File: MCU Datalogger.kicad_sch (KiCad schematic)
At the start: 25 parts, among them U1 24LC1025, U2 DS1337S+, U3 24LC1025, U4 ATMEGA328P-AU, Y1 32.768 KHz, Y2 16MHz

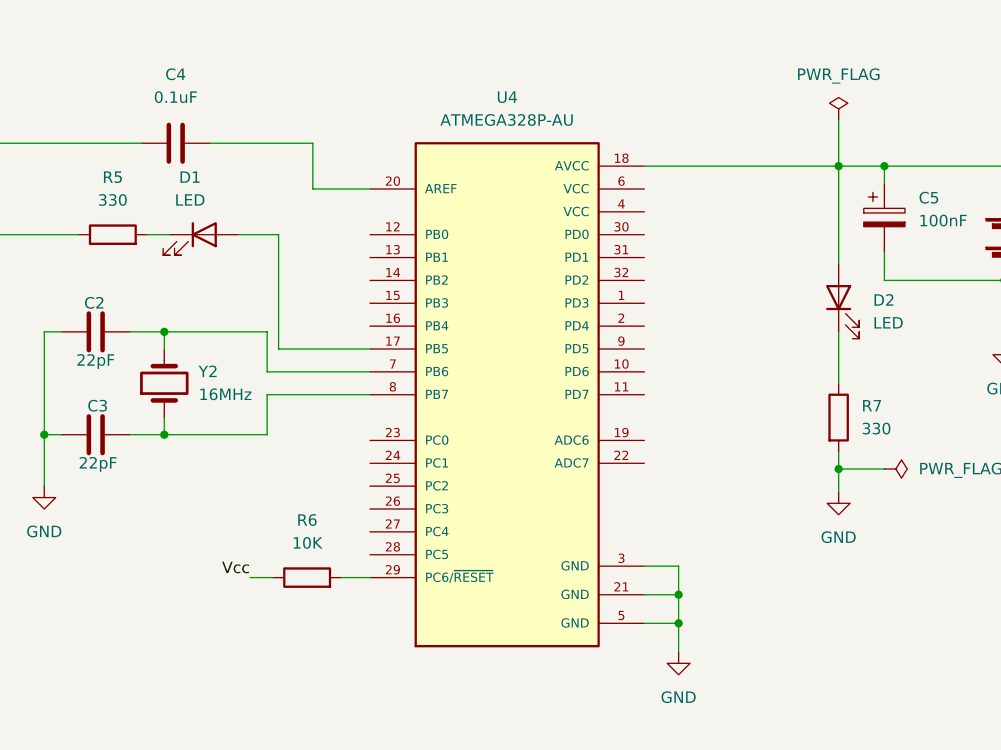
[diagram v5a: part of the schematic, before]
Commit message: finished wiring of main sheet
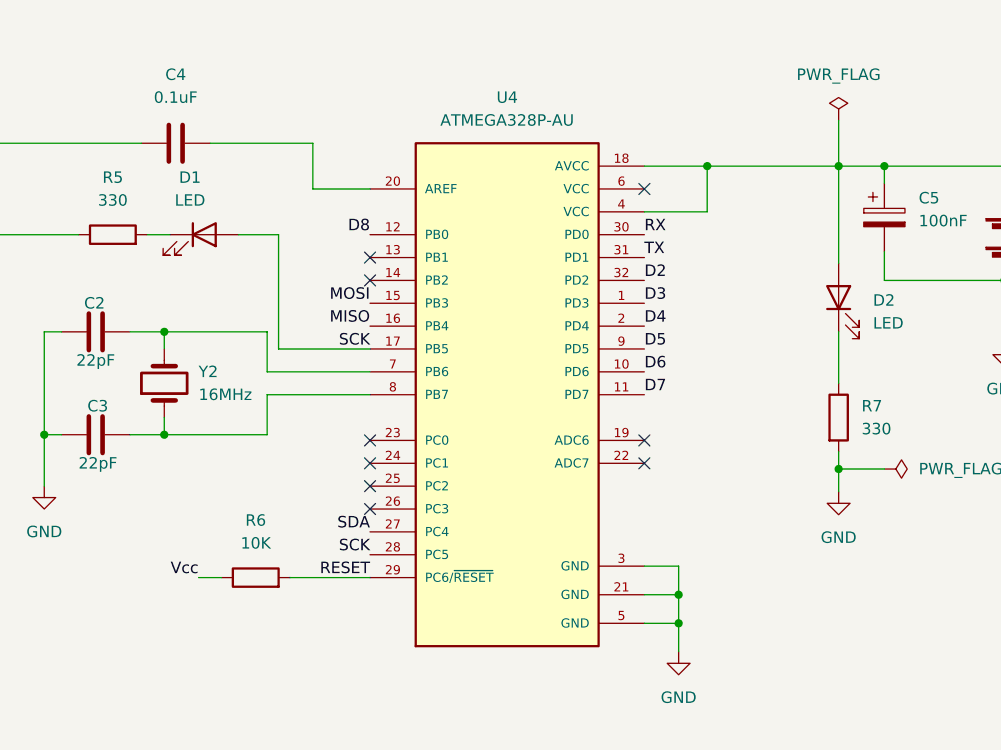
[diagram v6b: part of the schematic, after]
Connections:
- net SCK: now also D1.2 (A), U4.17 (PB5), U4.28 (PC5)
- net SDA: now also U4.27 (PC4)
- net at BT1.1 (+), C5.1, D2.2 (A)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: now also U4.4 (VCC)
- net D3: now reaches U4.1 (PD3)
- net D6: now reaches U4.10 (PD6)
- net D7: now reaches U4.11 (PD7)
- net D8: now reaches U4.12 (PB0)
- net MOSI: now reaches U4.15 (PB3)
- net MISO: now reaches U4.16 (PB4)
- net D4: now reaches U4.2 (PD4)
- net RESET: now reaches R6.2, U4.29 (PC6/~{RESET})
- net RX: now reaches U4.30 (PD0)
- net TX: now reaches U4.31 (PD1)
- net D2: now reaches U4.32 (PD2)
- net D5: now reaches U4.9 (PD5)
- no-connect marks 0 -> 9
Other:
- moved on the sheet: R6
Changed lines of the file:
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@@
   (junction (at 155.575 49.53) (diameter 0) (color 0 0 0 0)
   )
+  (junction (at 238.125 41.91) (diameter 0) (color 0 0 0 0)
+  )
   (junction (at 271.145 54.61) (diameter 0) (color 0 0 0 0)
   )
   (junction (at 88.9 26.67) (diameter 0) (color 0 0 0 0)
   )
+  (no_connect (at 200.66 52.07))
+  (no_connect (at 200.66 54.61))
+  (no_connect (at 200.66 72.39))
+  (no_connect (at 200.66 74.93))
+  (no_connect (at 200.66 77.47))
+  (no_connect (at 200.66 80.01))
+  (no_connect (at 231.14 44.45))
+  (no_connect (at 231.14 72.39))
+  (no_connect (at 231.14 74.93))
   (wire (pts (xy 234.95 92.71) (xy 234.95 95.885))
     (stroke (width 0) (type default) (color 0 0 0 0))
@@
     (stroke (width 0) (type default) (color 0 0 0 0))
   )
-  (wire (pts (xy 187.325 87.63) (xy 189.865 87.63))
+  (wire (pts (xy 181.61 87.63) (xy 184.15 87.63))
     (stroke (width 0) (type default) (color 0 0 0 0))
   )
@@
     (stroke (width 0) (type default) (color 0 0 0 0))
   )
+  (wire (pts (xy 231.14 46.99) (xy 238.125 46.99))
+    (stroke (width 0) (type default) (color 0 0 0 0))
+  )
   (wire (pts (xy 99.06 34.29) (xy 99.06 45.72))
     (stroke (width 0) (type default) (color 0 0 0 0))
@@
     (stroke (width 0) (type default) (color 0 0 0 0))
   )
+  (wire (pts (xy 238.125 41.91) (xy 252.73 41.91))
+    (stroke (width 0) (type default) (color 0 0 0 0))
+  )
   (wire (pts (xy 74.93 35.56) (xy 88.9 35.56))
     (stroke (width 0) (type default) (color 0 0 0 0))
@@
     (stroke (width 0) (type default) (color 0 0 0 0))
   )
-  (wire (pts (xy 197.485 87.63) (xy 200.66 87.63))
+  (wire (pts (xy 191.77 87.63) (xy 200.66 87.63))
     (stroke (width 0) (type default) (color 0 0 0 0))
   )
@@
     (stroke (width 0) (type default) (color 0 0 0 0))
   )
-  (wire (pts (xy 231.14 41.91) (xy 252.73 41.91))
+  (wire (pts (xy 231.14 41.91) (xy 238.125 41.91))
     (stroke (width 0) (type default) (color 0 0 0 0))
   )
@@
     (stroke (width 0) (type default) (color 0 0 0 0))
   )
+  (wire (pts (xy 238.125 46.99) (xy 238.125 41.91))
+    (stroke (width 0) (type default) (color 0 0 0 0))
+  )
   (wire (pts (xy 164.465 71.755) (xy 164.465 77.47))
     (stroke (width 0) (type default) (color 0 0 0 0))
@@
     (effects (font (size 1.27 1.27)) (justify right bottom))
   )
+  (label "D5" (at 231.14 62.23 0)
+    (effects (font (size 1.27 1.27)) (justify left bottom))
+  )
+  (label "D6" (at 231.14 64.77 0)
+    (effects (font (size 1.27 1.27)) (justify left bottom))
+  )
   (label "SCK" (at 86.36 177.8 180)
     (effects (font (size 1.27 1.27)) (justify right bottom))
   )
+  (label "TX" (at 231.14 52.07 0)
+    (effects (font (size 1.27 1.27)) (justify left bottom))
+  )
+  (label "SDA" (at 200.66 82.55 180)
+    (effects (font (size 1.27 1.27)) (justify right bottom))
+  )
   (label "Vcc" (at 52.07 172.72 180)
     (effects (font (size 1.27 1.27)) (justify right bottom))
   )
+  (label "SCK" (at 200.66 85.09 180)
+    (effects (font (size 1.27 1.27)) (justify right bottom))
+  )
+  (label "MISO" (at 200.66 59.69 180)
+    (effects (font (size 1.27 1.27)) (justify right bottom))
+  )
   (label "Vcc" (at 22.86 167.64 180)
     (effects (font (size 1.27 1.27)) (justify right bottom))
   )
+  (label "D4" (at 231.14 59.69 0)
+    (effects (font (size 1.27 1.27)) (justify left bottom))
+  )
+  (label "RESET" (at 200.66 87.63 180)
+    (effects (font (size 1.27 1.27)) (justify right bottom))
+  )
   (label "Vcc" (at 33.02 162.56 0)
     (effects (font (size 1.27 1.27)) (justify left bottom))
   )
+  (label "RX" (at 231.14 49.53 0)
+    (effects (font (size 1.27 1.27)) (justify left bottom))
+  )
+  (label "MOSI" (at 200.66 57.15 180)
+    (effects (font (size 1.27 1.27)) (justify right bottom))
+  )
   (label "Vcc" (at 22.86 172.72 180)
     (effects (font (size 1.27 1.27)) (justify right bottom))
@@
     (effects (font (size 1.27 1.27)) (justify right bottom))
   )
+  (label "D7" (at 231.14 67.31 0)
+    (effects (font (size 1.27 1.27)) (justify left bottom))
+  )
   (label "SDA" (at 36.83 39.37 180)
     (effects (font (size 1.27 1.27)) (justify right bottom))
@@
     (effects (font (size 1.27 1.27)) (justify right bottom))
   )
+  (label "D3" (at 231.14 57.15 0)
+    (effects (font (size 1.27 1.27)) (justify left bottom))
+  )
+  (label "SCK" (at 200.66 62.23 180)
+    (effects (font (size 1.27 1.27)) (justify right bottom))
+  )
+  (label "D8" (at 200.66 49.53 180)
+    (effects (font (size 1.27 1.27)) (justify right bottom))
+  )
   (label "SDA" (at 72.39 167.64 0)
     (effects (font (size 1.27 1.27)) (justify left bottom))
   )
+  (label "D2" (at 231.14 54.61 0)
+    (effects (font (size 1.27 1.27)) (justify left bottom))
+  )
   (label "Vcc" (at 62.23 162.56 0)
     (effects (font (size 1.27 1.27)) (justify left bottom))
   )
-  (label "Vcc" (at 187.325 87.63 180)
+  (label "Vcc" (at 181.61 87.63 180)
     (effects (font (size 1.27 1.27)) (justify right bottom))
   )
@@
     (pin "1")
   )
-  (symbol (lib_id "Device:R") (at 193.675 87.63 90) (unit 1)
-    (in_bom yes) (on_board yes) (fields_autoplaced)
-    (property "Reference" "R6" (id 0) (at 193.675 81.28 90))
-    (property "Value" "10K" (id 1) (at 193.675 83.82 90))
-    (property "Footprint" "Resistor_SMD:R_0805_2012Metric" (id 2) (at 193.675 89.408 90)
-      (effects (font (size 1.27 1.27)) hide)
-    )
-    (property "Datasheet" "~" (id 3) (at 193.675 87.63 0)
-      (effects (font (size 1.27 1.27)) hide)
-    )
+  (symbol (lib_id "Device:R") (at 187.96 87.63 90) (unit 1)
+    (in_bom yes) (on_board yes) (fields_autoplaced)
+    (property "Reference" "R6" (id 0) (at 187.96 81.28 90))
+    (property "Value" "10K" (id 1) (at 187.96 83.82 90))
+    (property "Footprint" "Resistor_SMD:R_0805_2012Metric" (id 2) (at 187.96 89.408 90)
+      (effects (font (size 1.27 1.27)) hide)
+    )
+    (property "Datasheet" "~" (id 3) (at 187.96 87.63 0)
+      (effects (font (size 1.27 1.27)) hide)
+    )

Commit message: finished wiring everything up.
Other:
- sheet Connectors ports: added D2, D3, D4, D5, D6, D7, D8, GND, MISO, MOSI, RESET, RX, SCK, SDA, TX, Vcc; removed none

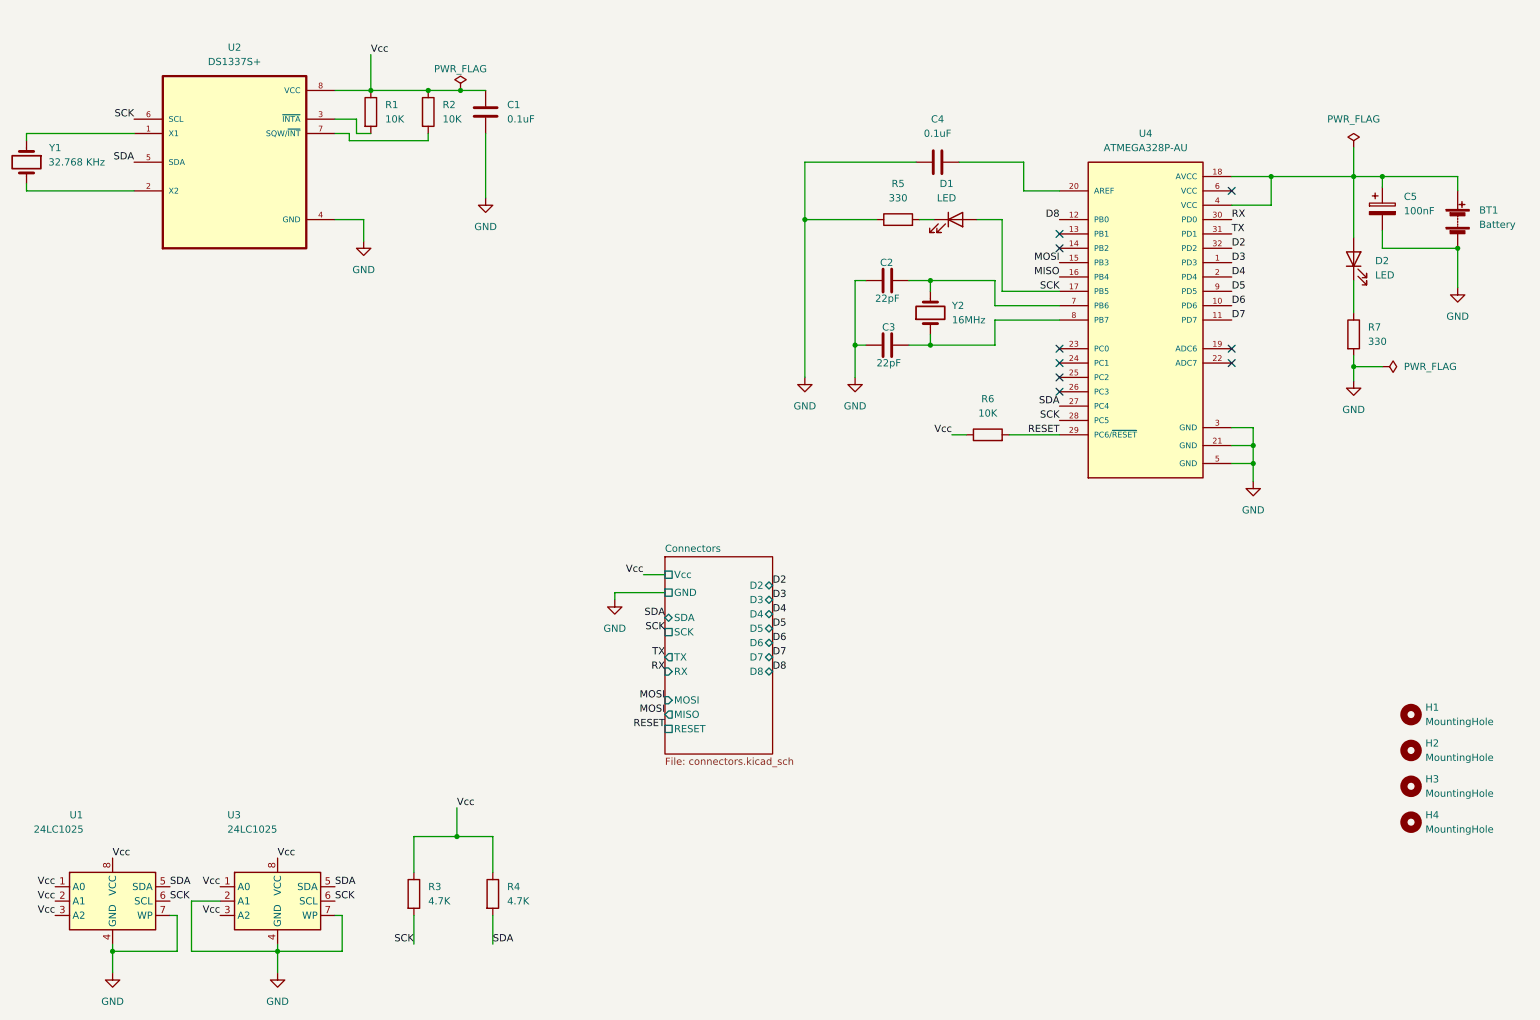
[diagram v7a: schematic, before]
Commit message: Add Comments and boxes around the different groups of components
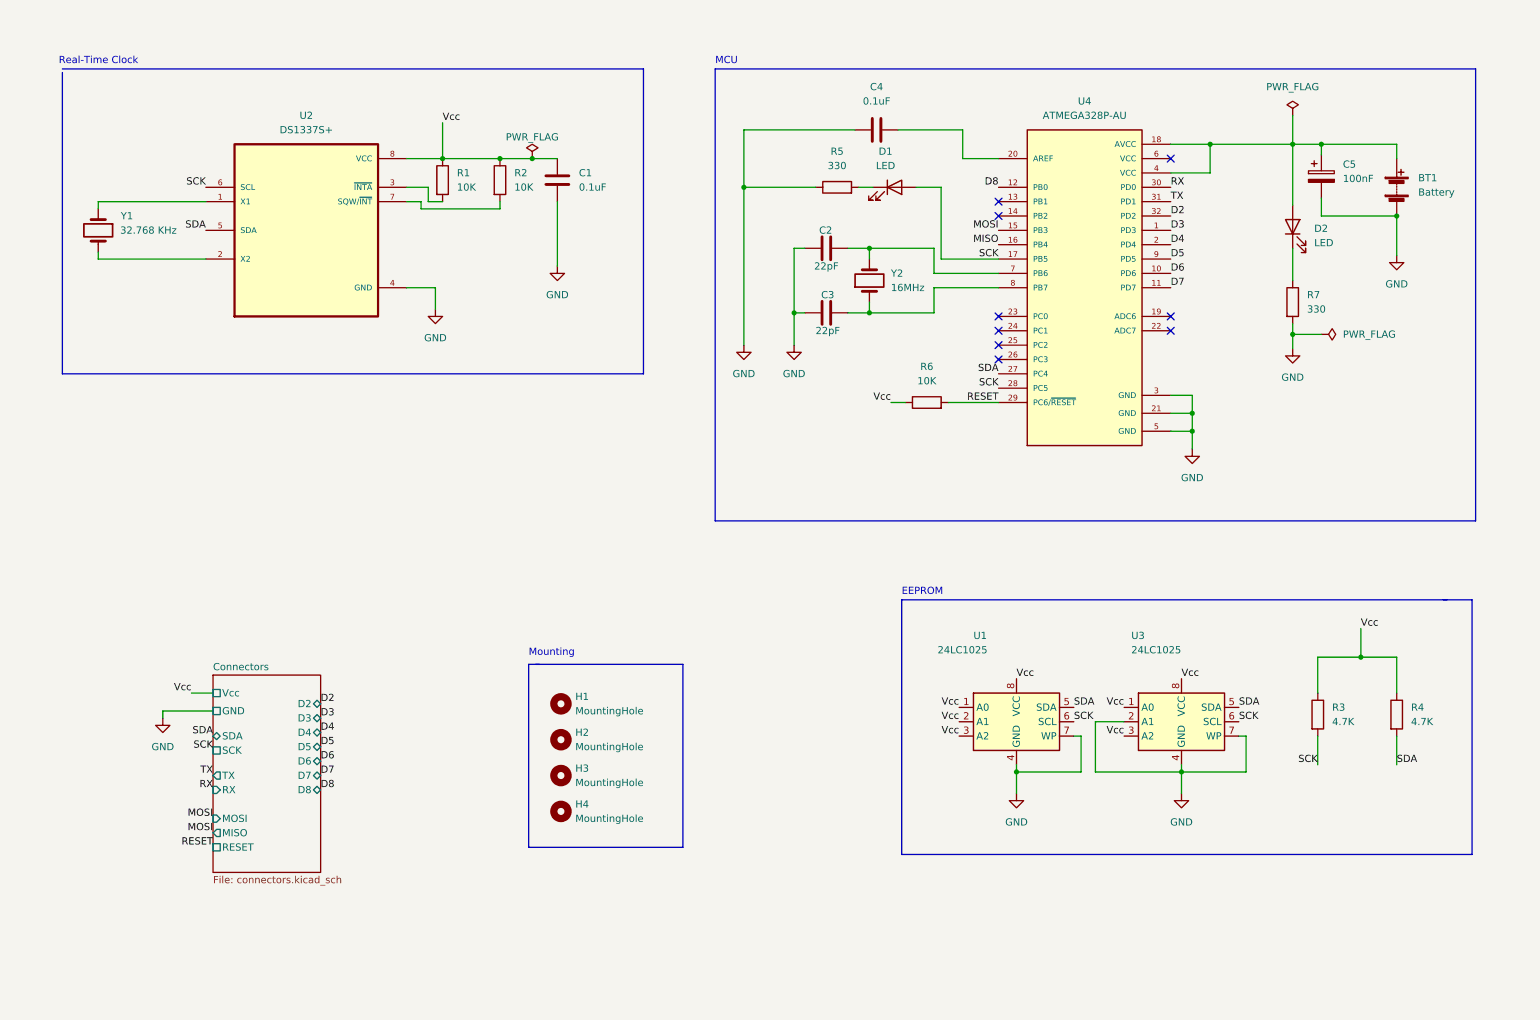
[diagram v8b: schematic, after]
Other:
- note added: "EEPROM"
- note added: "MCU"
- note added: "Mounting"
- note added: "Real-Time Clock"
- moved on the sheet: BT1, C1, C2, C3, C4, C5, D1, D2, H1, H2, H3, H4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
